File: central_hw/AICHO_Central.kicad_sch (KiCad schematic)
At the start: 20 parts, among them J1 DC D5.5, U1 TPS54302, U2 XC6206P332MR, U3 RP2040, U4 TM8211

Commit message: central_hw: Schematic for Orange Pi Zero stand-in
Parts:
- removed C21, C22: 1u, Capacitor_SMD:C_0402_1005Metric, symbol Device:C
- removed U2: XC6206P332MR, Package_TO_SOT_SMD:SOT-23-3, symbol Regulator_Linear:XC6206PxxxMR
- removed U3: RP2040, Package_DFN_QFN:QFN-56-1EP_7x7mm_P0.4mm_EP3.2x3.2mm, symbol MCU_RaspberryPi:RP2040
- removed U4: TM8211, Package_SO:SOP-8_3.9x4.9mm_P1.27mm, symbol TM8211:TM8211
- added C21, C22, C23, C24: 100u 50V, Capacitor_SMD:CP_Elec_6.3x7.7, symbol Device:C_Polarized
- added J2: P2.54 2x20, Connector_PinHeader_2.54mm:PinHeader_2x20_P2.54mm_Vertical, symbol Connector_Generic:Conn_02x20_Odd_Even
- added J21, J22, J23, J24: PH2.0, Connector_JST:JST_PH_S3B-PH-SM4-TB_1x03-1MP_P2.00mm_Horizontal, symbol Connector_Generic_MountingPin:Conn_01x03_MountingPin
- added J3: P2.54 1x03, Connector_PinSocket_2.54mm:PinSocket_1x03_P2.54mm_Vertical, symbol Connector_Generic:Conn_01x03
- C17: value 47p -> 75p
- C18: value 100u 50V -> 470u 10V
- R12: value 39k -> 27k
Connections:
- net +24V: now also C21.1, C22.1, C23.1, C24.1, J21.1 (Pin_1), J22.1 (Pin_1), J23.1 (Pin_1), J24.1 (Pin_1); no longer C18.1
- net GND: now also C21.2, C22.2, C23.2, C24.2, J2.14 (Pin_14), J2.20 (Pin_20), J2.25 (Pin_25), J2.30 (Pin_30), J2.34 (Pin_34), J2.39 (Pin_39), J2.6 (Pin_6), J2.9 (Pin_9), J21.2 (Pin_2), J21.MP (MountPin), J22.2 (Pin_2), J22.MP (MountPin), J23.2 (Pin_2), J23.MP (MountPin), J24.2 (Pin_2), J24.MP (MountPin), J3.1 (Pin_1)
- net +5V: now reaches C15.1, C16.1, C17.1, L1.2, R11.1
- net +5V: now also C18.1, J2.2 (Pin_2), J2.4 (Pin_4)
- new net UART_0_RX: J2.10 (Pin_10), J3.3 (Pin_3)
- new net UART_0_TX: J2.8 (Pin_8), J3.2 (Pin_2)
- new net UART_2: J2.15 (Pin_15), J2.22 (Pin_22), J21.3 (Pin_3)
- new net UART_3: J2.27 (Pin_27), J2.28 (Pin_28), J22.3 (Pin_3)
- new net UART_4: J2.16 (Pin_16), J2.7 (Pin_7), J23.3 (Pin_3)
- new net UART_5: J2.11 (Pin_11), J2.13 (Pin_13), J24.3 (Pin_3)
- no-connect marks 2 -> 22
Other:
- note removed: "3.652 V"

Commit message: central_hw: Layout & routing
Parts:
- added H1, H2, H3, H4: MountingHole, MountingHole:MountingHole_2.2mm_M2_Pad_Via, symbol Mechanical:MountingHole
- added J31, J32, J33, J34: PH2.0, Connector_JST:JST_PH_S2B-PH-SM4-TB_1x02-1MP_P2.00mm_Horizontal, symbol Connector_Generic_MountingPin:Conn_01x02_MountingPin
- added R31, R32, R33, R34: 100k, Resistor_SMD:R_0402_1005Metric, symbol Device:R
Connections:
- net GND: now also J31.2 (Pin_2), J31.MP (MountPin), J32.2 (Pin_2), J32.MP (MountPin), J33.2 (Pin_2), J33.MP (MountPin), J34.2 (Pin_2), J34.MP (MountPin)
- net UART_2: now also J22.3 (Pin_3); no longer J21.3 (Pin_3)
- net UART_3: now also J21.3 (Pin_3); no longer J22.3 (Pin_3)
- net UART_4: now also J24.3 (Pin_3); no longer J23.3 (Pin_3)
- net UART_5: now also J23.3 (Pin_3); no longer J24.3 (Pin_3)
- net +3.3V: now reaches J2.1 (Pin_1)
- net +3.3V: now also J2.17 (Pin_17), R31.1, R32.1, R33.1, R34.1
- net BTN_C: now reaches J2.19 (Pin_19)
- net BTN_C: now also J33.1 (Pin_1), R33.2
- net BTN_B: now reaches J2.26 (Pin_26)
- net BTN_B: now also J32.1 (Pin_1), R32.2
- net BTN_D: now reaches J2.3 (Pin_3)
- net BTN_D: now also J34.1 (Pin_1), R34.2
- net BTN_A: now reaches J2.40 (Pin_40)
- net BTN_A: now also J31.1 (Pin_1), R31.2
- no-connect marks 22 -> 16
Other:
- moved on the sheet: C22, C23, C24, J22, J23, J24

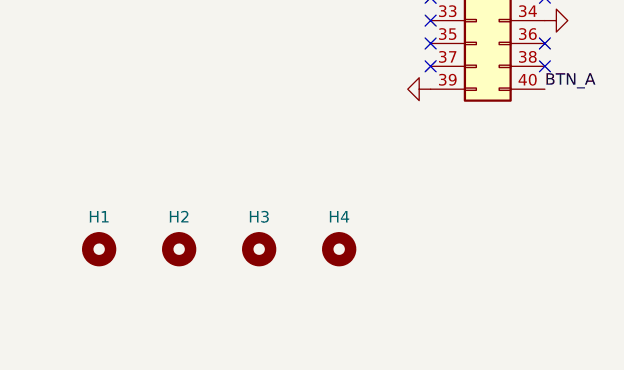
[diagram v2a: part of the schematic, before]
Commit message: central_hw: Edit silkscreen & finalize
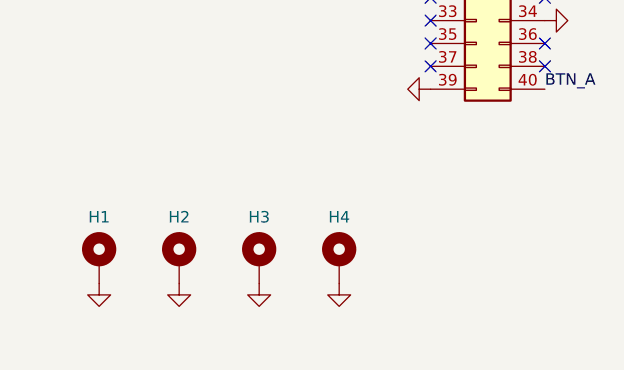
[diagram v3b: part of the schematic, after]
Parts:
- H1, H2, H3, H4: symbol Mechanical:MountingHole -> Mechanical:MountingHole_Pad
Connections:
- net GND: now also H1.1, H2.1, H3.1, H4.1
